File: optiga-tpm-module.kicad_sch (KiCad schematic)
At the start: 40 parts, among them J1 Plug_Samtec_ERM5_2x20_ERM5-02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, U1 SLB9672XU20FW1624XTMA1

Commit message: [#104798] Change PCB stackup, clean up vias and traces according to review
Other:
- moved on the sheet: D1, R12, TP11
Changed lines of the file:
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@@
 	)
 	(junction
-		(at 92.71 115.57)
+		(at 96.52 115.57)
 		(diameter 0)
 		(color 0 0 0 0)
@@
 	(wire
 		(pts
-			(xy 92.71 114.3) (xy 92.71 115.57)
+			(xy 96.52 114.3) (xy 96.52 115.57)
 		)
 		(stroke
@@
 	(wire
 		(pts
-			(xy 92.71 115.57) (xy 92.71 118.11)
+			(xy 96.52 115.57) (xy 96.52 118.11)
 		)
 		(stroke
@@
 	(wire
 		(pts
-			(xy 92.71 115.57) (xy 135.89 115.57)
+			(xy 96.52 115.57) (xy 135.89 115.57)
 		)
 		(stroke
@@
 	(wire
 		(pts
-			(xy 92.71 123.19) (xy 92.71 124.46)
+			(xy 96.52 123.19) (xy 96.52 124.46)
 		)
 		(stroke
@@
 	(wire
 		(pts
-			(xy 92.71 129.54) (xy 92.71 132.08)
+			(xy 96.52 129.54) (xy 96.52 132.08)
 		)
 		(stroke
@@
 	(symbol
 		(lib_id "antmicroLEDIndicationDiscrete:LED_G_0603_KP-1608CGCK")
-		(at 92.71 129.54 90)
+		(at 96.52 129.54 90)
 		(unit 1)
 		(body_style 1)
@@
 		(dnp no)
 		(property "Reference" "D1"
-			(at 86.36 125.73 90)
+			(at 90.17 125.73 90)
 			(show_name no)
 			(do_not_autoplace no)
@@
 		)
 		(property "Value" "LED_G_0603_KP-1608CGCK"
-			(at 100.33 106.68 0)
+			(at 104.14 106.68 0)
 			(hide yes)
 			(show_name no)
@@
 		)
 		(property "Footprint" "antmicro-footprints:LED_0603_1608Metric_G"
-			(at 102.87 106.68 0)
+			(at 106.68 106.68 0)
 			(hide yes)
 			(show_name no)
@@
 		)
 		(property "Datasheet" "http://www.kingbright.com/attachments/file/psearch//000/00/00/KP-1608CGCK(Ver.23B).pdf"
-			(at 105.41 106.68 0)
+			(at 109.22 106.68 0)
 			(hide yes)
 			(show_name no)
@@
 		)
 		(property "Description" ""
-			(at 92.71 129.54 0)
+			(at 96.52 129.54 0)
 			(hide yes)
 			(show_name no)
@@
 		)
 		(property "MPN" "KP-1608CGCK"
-			(at 107.95 106.68 0)
+			(at 111.76 106.68 0)
 			(hide yes)
 			(show_name no)
@@
 		)
 		(property "Manufacturer" "Kingbright"
-			(at 110.49 106.68 0)
+			(at 114.3 106.68 0)
 			(hide yes)
 			(show_name no)
@@
 		)
 		(property "Color" "Green"
-			(at 86.36 128.27 90)
+			(at 90.17 128.27 90)
 			(show_name no)
 			(do_not_autoplace no)
@@
 		)
 		(property "Author" "Antmicro"
-			(at 113.03 106.68 0)
+			(at 116.84 106.68 0)
 			(hide yes)
 			(show_name no)
@@
 		)
 		(property "License" "Apache-2.0"
-			(at 115.57 106.68 0)
+			(at 119.38 106.68 0)
 			(hide yes)
 			(show_name no)
@@
 	(symbol
 		(lib_id "antmicropower:GND")
-		(at 92.71 132.08 0)
+		(at 96.52 132.08 0)
 		(unit 1)
 		(body_style 1)
@@
 		(fields_autoplaced yes)
 		(property "Reference" "#PWR09"
-			(at 101.6 134.62 0)
+			(at 105.41 134.62 0)
 			(hide yes)
 			(show_name no)
@@
 		)
 		(property "Value" "GND"
-			(at 90.6998 137.16 0)
+			(at 94.5098 137.16 0)
 			(show_name no)
 			(do_not_autoplace no)
@@
 		)
 		(property "Footprint" ""
-			(at 101.6 139.7 0)
+			(at 105.41 139.7 0)
 			(hide yes)
 			(show_name no)
@@
 		)
 		(property "Datasheet" ""
-			(at 101.6 144.78 0)
+			(at 105.41 144.78 0)
 			(hide yes)
 			(show_name no)
@@
 		)
 		(property "Description" ""
-			(at 92.71 132.08 0)
+			(at 96.52 132.08 0)
 			(hide yes)
 			(show_name no)
@@
 		)
 		(property "Author" "Antmicro"
-			(at 101.6 139.7 0)
+			(at 105.41 139.7 0)
 			(hide yes)
 			(show_name no)
@@
 		)
 		(property "License" "Apache-2.0"
-			(at 101.6 142.24 0)
+			(at 105.41 142.24 0)
 			(hide yes)
 			(show_name no)
@@
 	(symbol
 		(lib_id "antmicroResistors0402:R_470R_0402")
-		(at 92.71 123.19 90)
+		(at 96.52 123.19 90)
 		(unit 1)
 		(body_style 1)
@@
 		(fields_autoplaced yes)
 		(property "Reference" "R12"
-			(at 90.17 119.3799 90)
+			(at 93.98 119.3799 90)
 			(show_name no)
 			(do_not_autoplace no)
@@
 		)
 		(property "Value" "R_470R_0402"
-			(at 105.41 102.87 0)
+			(at 109.22 102.87 0)
 			(hide yes)
 			(show_name no)
@@
 		)
 		(property "Footprint" "antmicro-footprints:R_0402_1005Metric"
-			(at 107.95 102.87 0)
+			(at 111.76 102.87 0)
 			(hide yes)
 			(show_name no)
@@
 		)
 		(property "Datasheet" "https://www.bourns.com/docs/product-datasheets/cr.pdf"
-			(at 110.49 102.87 0)
+			(at 114.3 102.87 0)
 			(hide yes)
 			(show_name no)
@@
 		)
 		(property "Description" ""
-			(at 92.71 123.19 0)
+			(at 96.52 123.19 0)
 			(hide yes)
 			(show_name no)
@@
 		)
 		(property "Manufacturer" "Bourns"
-			(at 115.57 102.87 0)
+			(at 119.38 102.87 0)
 			(hide yes)
 			(show_name no)
@@
 		)
 		(property "MPN" "CR0402-FX-4700GLF"
-			(at 113.03 102.87 0)
+			(at 116.84 102.87 0)
 			(hide yes)
 			(show_name no)
@@
 		)
 		(property "Val" "470R"
-			(at 90.17 121.9199 90)
+			(at 93.98 121.9199 90)
 			(show_name no)
 			(do_not_autoplace no)
@@
 		)
 		(property "License" "Apache-2.0"
-			(at 118.11 102.87 0)
+			(at 121.92 102.87 0)
 			(hide yes)
 			(show_name no)
@@
 		)
 		(property "Author" "Antmicro"
-			(at 120.65 102.87 0)
+			(at 124.46 102.87 0)
 			(hide yes)
 			(show_name no)
@@
 		)
 		(property "Tolerance" "1%"
-			(at 102.87 102.87 0)
+			(at 106.68 102.87 0)
 			(hide yes)
 			(show_name no)
@@
 	(symbol
 		(lib_id "antmicroTestPoints:TP_0.75mm_SMD")
-		(at 92.71 114.3 270)
+		(at 96.52 114.3 270)
 		(mirror x)
 		(unit 1)
@@
 		(dnp no)
 		(property "Reference" "TP11"
-			(at 92.71 107.442 0)
+			(at 96.52 107.442 0)
 			(show_name no)
 			(do_not_autoplace no)
@@
 		)
 		(property "Value" "TP_0.75mm_SMD"
-			(at 88.9 104.14 0)
+			(at 92.71 104.14 0)
 			(hide yes)
 			(show_name no)
@@
 		)
 		(property "Footprint" "antmicro-footprints:TP_SMD_0.75mm"
-			(at 86.36 104.14 0)
+			(at 90.17 104.14 0)
 			(hide yes)
 			(show_name no)
@@
 		)
 		(property "Datasheet" ""
-			(at 80.01 96.52 0)
+			(at 83.82 96.52 0)
 			(hide yes)
 			(show_name no)
@@
 		)
 		(property "Description" "SMT test point"
-			(at 78.74 103.505 0)
+			(at 82.55 103.505 0)
 			(hide yes)
 			(show_name no)
@@
 		)
 		(property "MPN" ""
-			(at 81.28 103.505 0)
+			(at 85.09 103.505 0)
 			(hide yes)
 			(show_name no)
@@
 		)
 		(property "Manufacturer" ""
-			(at 86.36 103.505 0)
+			(at 90.17 103.505 0)
 			(hide yes)
 			(show_name no)
@@
 		)
 		(property "Author" "Antmicro"
-			(at 83.82 104.14 0)
+			(at 87.63 104.14 0)
 			(hide yes)
 			(show_name no)
@@
 		)
 		(property "License" "Apache-2.0"
-			(at 81.28 104.14 0)
+			(at 85.09 104.14 0)
 			(hide yes)
 			(show_name no)

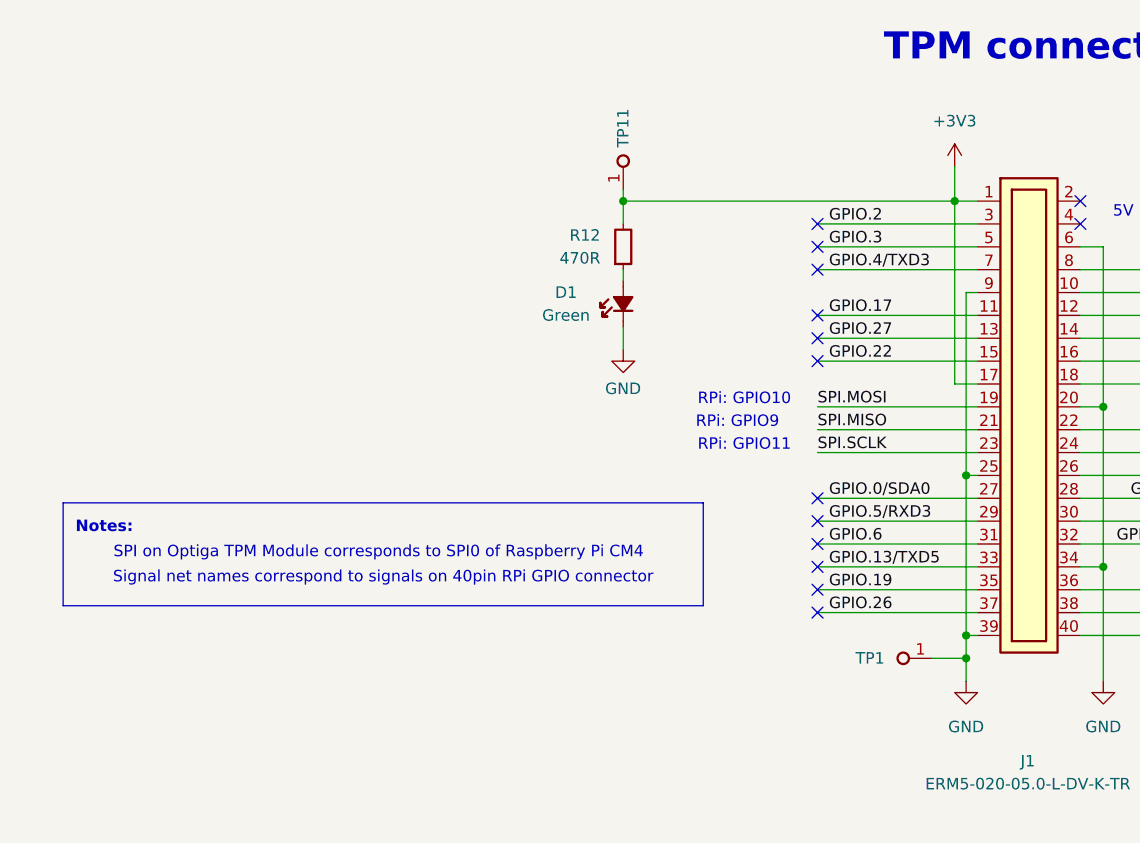
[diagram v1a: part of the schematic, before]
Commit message: [#104798] Clean up the schematic, add termal vias to IC
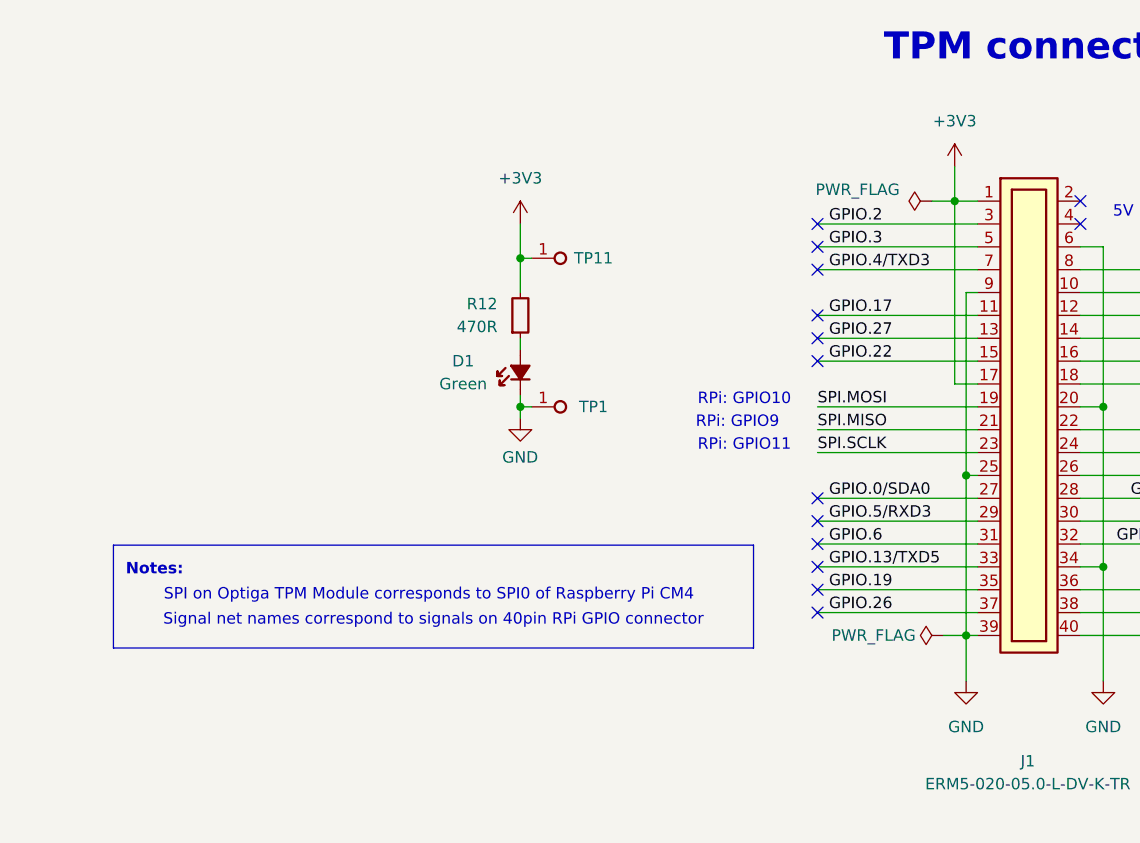
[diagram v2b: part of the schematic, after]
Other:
- moved on the sheet: D1, R12, TP11
